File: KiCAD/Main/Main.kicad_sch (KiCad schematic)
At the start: 0 parts

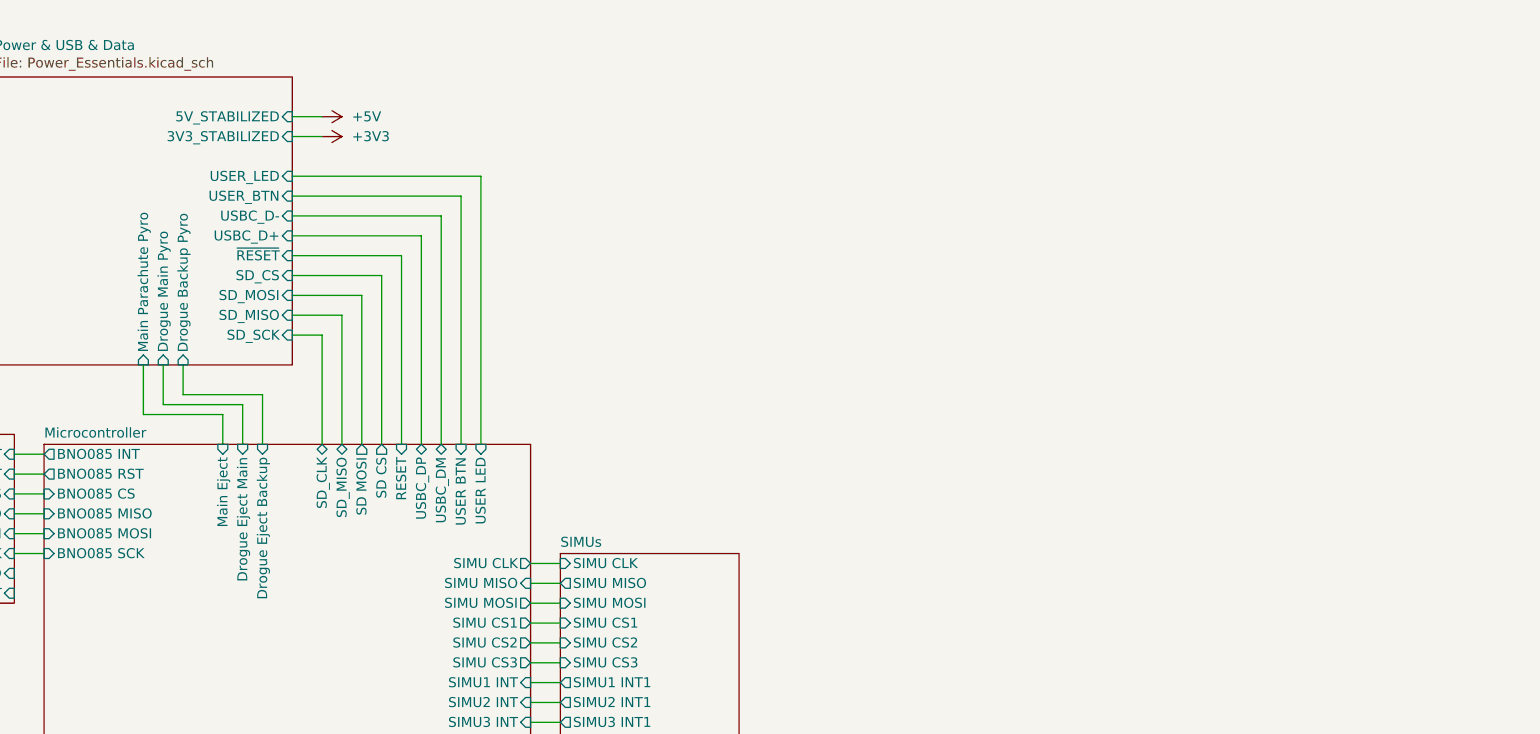
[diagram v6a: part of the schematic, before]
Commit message: Create wiring diagram draft
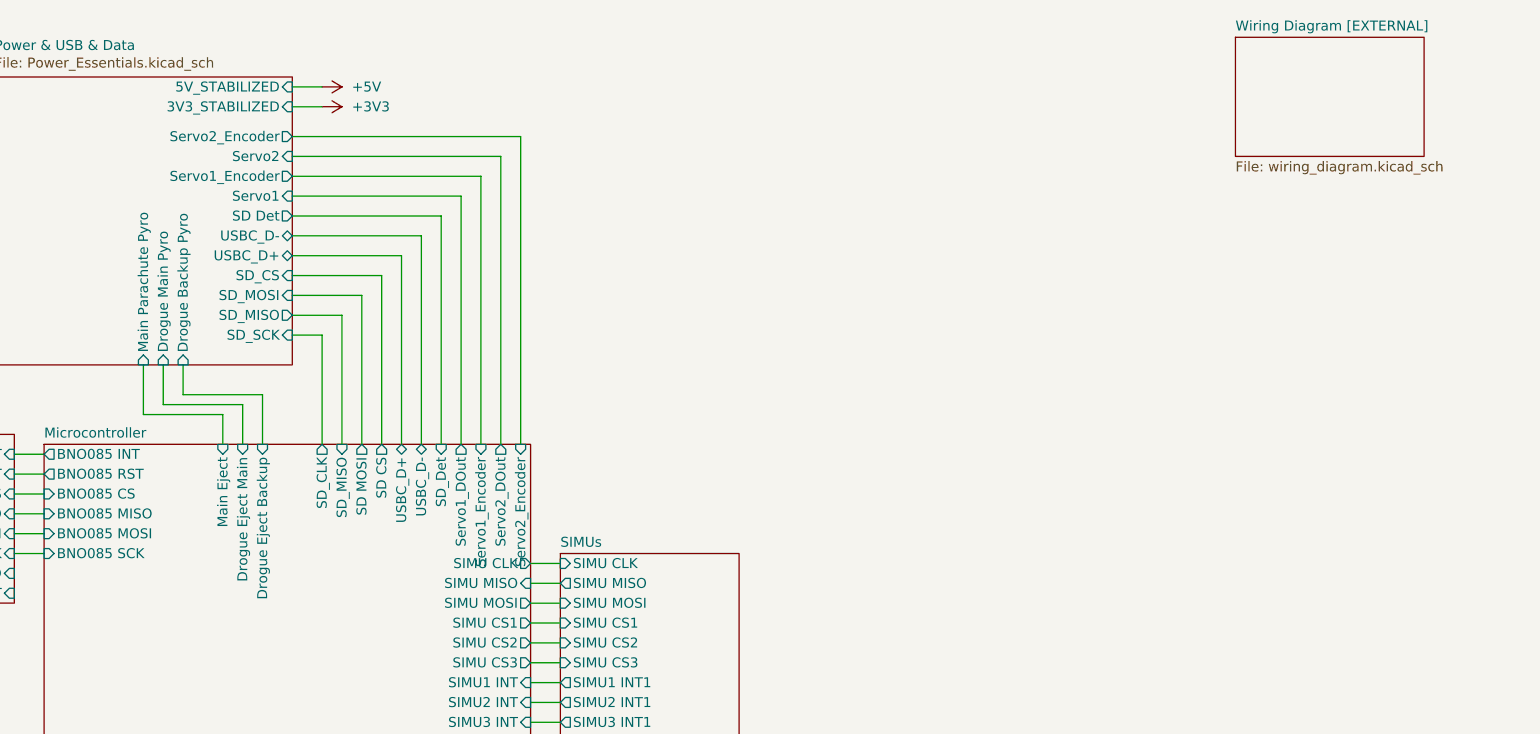
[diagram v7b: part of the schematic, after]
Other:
- added sheet Wiring Diagram [EXTERNAL] (wiring_diagram.kicad_sch)
- sheet Microcontroller ports: added SD_Det, Servo1_DOut, Servo1_Encoder, Servo2_DOut, Servo2_Encoder, USBC_D+, USBC_D-; removed RESET, USBC_DM, USBC_DP, USER BTN, USER LED
- sheet Power & USB & Data ports: added SD Det, Servo1, Servo1_Encoder, Servo2, Servo2_Encoder; removed USER_BTN, USER_LED, ~{RESET}

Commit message: Submit design for review
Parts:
- added D6: MBRS340, Diode_SMD:D_SMC, symbol Diode:MBRS340
- added J7: Conn_02x05_Top_Bottom_MountingPin, symbol Connector_Generic_MountingPin:Conn_02x05_Top_Bottom_MountingPin
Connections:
- net +3V3: now also J7.4 (Pin_4), J7.9 (Pin_9)
- net +5V: now also D6.1 (K)
- new net: D6.2 (A), J7.10 (Pin_10), J7.5 (Pin_5)
- new net GND: J7.3 (Pin_3), J7.8 (Pin_8)
- new net Microcontroller/DEBUG_JTMS-SWCLK: J7.6 (Pin_6)
- new net Microcontroller/DEBUG_JTMS-SWDIO: J7.7 (Pin_7)
- new net ~{RESET}: J7.1 (Pin_1)
- no-connect marks 0 -> 1
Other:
- sheet IMUs ports: added none; removed BNO_BOOT, BNO_CLKSELD, BNO_RST
- sheet Microcontroller ports: added DEBUG_JTMS-SWCLK, DEBUG_JTMS-SWDIO, ~{RESET}; removed BNO085 RST
- sheet Power & USB & Data ports: added none; removed 3V3_STABILIZED, 5V_STABILIZED
